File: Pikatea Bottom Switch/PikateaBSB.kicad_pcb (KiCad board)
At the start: 2 copper layers, 20 parts, among them J1 Micro_SD_Card, J2 Conn_01x15, SW1 Rotary_Encoder_Switch, U1 AMS1117-3.3, U2 74LVC125APW,118

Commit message: rudimentary layout
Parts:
- removed K?2: KEYSW, random-keyboard-parts:Generic-Mounthole
- moved SW1 50.3 mm to (115.2, 56.4)
- moved MX4 45.2 mm to (174.0, 59.6)
- moved MX2 45.2 mm to (153.8, 59.6)
- moved J2 36.8 mm to (172.2, 48.0), turned to 90 degrees
- moved C1 36.5 mm to (138.4, 58.2)
- moved C2 34.3 mm to (124.4, 48.0)
- moved C4 34.3 mm to (143.2, 43.1)
- moved K?1 34.3 mm to (143.8, 40.0)
- moved R3 34.3 mm to (128.8, 48.0)
- moved U1 34.3 mm to (127.1, 42.5)
- moved R2 27.7 mm to (162.1, 57.1)
- moved R4 27.7 mm to (166.5, 57.1)
- moved C3 27.2 mm to (161.1, 53.7)
- moved R1 27.2 mm to (165.5, 53.7)
- moved U2 16.0 mm to (154.2, 47.4)
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
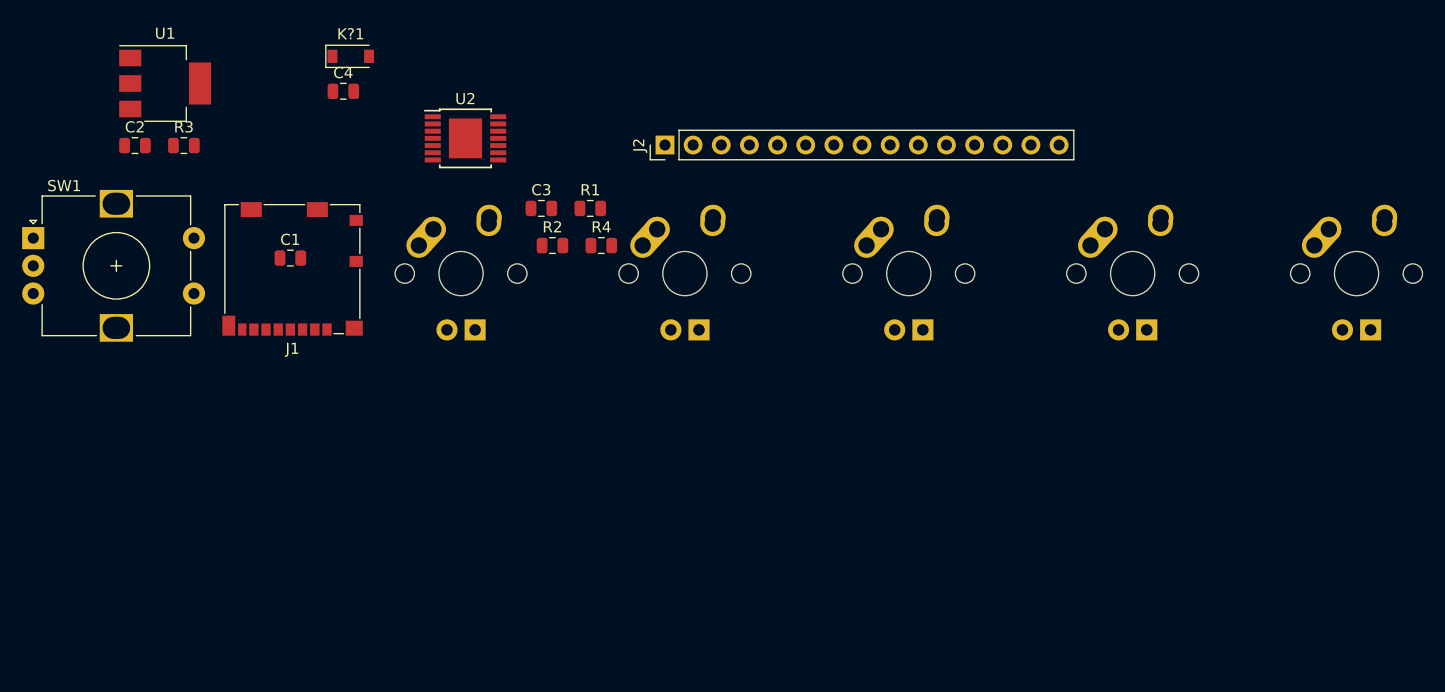
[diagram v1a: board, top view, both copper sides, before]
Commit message: Bottom Switch plate, footprints in place
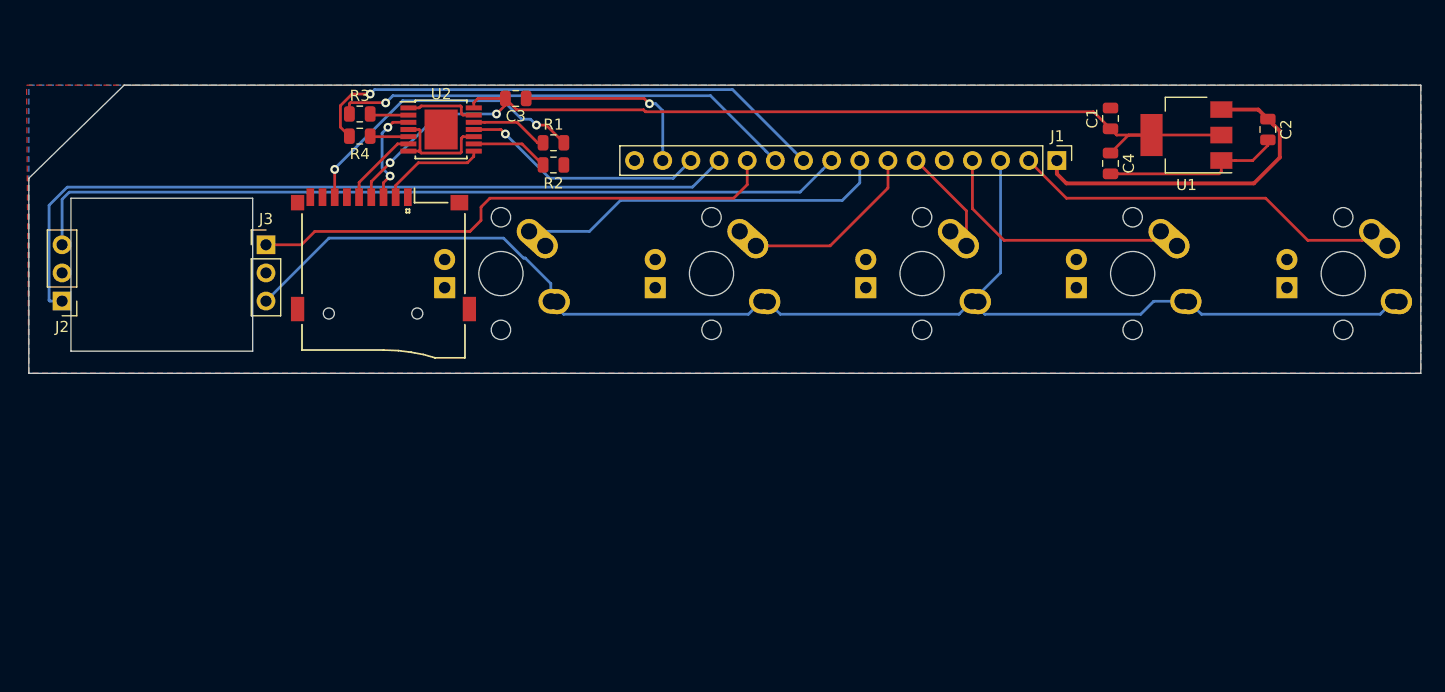
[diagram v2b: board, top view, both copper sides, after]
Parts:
- removed K?1: KEYSW, random-keyboard-parts:D_SOD-123-Pretty
- removed SW1: Rotary_Encoder_Switch, Rotary_Encoder:RotaryEncoder_Alps_EC12E-Switch_Vertical_H20mm
- added J3: Conn_01x03, Connector_PinHeader_2.54mm:PinHeader_1x03_P2.54mm_Vertical, F.Cu at (136.2, 57.0)
- added XS1: SD_ebay-uSD-push_push_SMD, Sd-Card:Conn_uSDcard, F.Cu at (146.8, 63.2)
- J1: value Micro_SD_Card -> Conn_01x16; footprint Connector_Card:microSD_HC_Molex_104031-0811 -> Connector_PinHeader_2.54mm:PinHeader_1x16_P2.54mm_Vertical
- J2: value Conn_01x15 -> Conn_01x03; footprint Connector_PinHeader_2.54mm:PinHeader_1x15_P2.54mm_Vertical -> Connector_PinHeader_2.54mm:PinHeader_1x03_P2.54mm_Vertical
- moved C2 102.2 mm to (226.6, 46.6), turned to 270 degrees
- moved U1 92.3 mm to (219.2, 47.1), turned to 180 degrees
- moved C1 75.1 mm to (212.4, 45.6), turned to 90 degrees
- moved J1 69.7 mm to (207.6, 49.4), turned to 270 degrees
- moved C4 69.5 mm to (212.4, 49.7), turned to 270 degrees
- moved J2 56.2 mm to (117.8, 62.1), turned to 180 degrees
- moved R4 23.9 mm to (144.7, 47.2)
- moved R3 16.1 mm to (144.7, 45.2)
- moved C3 10.2 mm to (158.7, 43.8)
- moved R2 7.27 mm to (162.1, 49.8), turned to 180 degrees
- moved R1 6.79 mm to (162.1, 47.8)
- moved MX2 3.60 mm to (157.4, 59.6), turned to 270 degrees
- moved MX4 2.40 mm to (176.4, 59.6), turned to 270 degrees
- moved U2 2.34 mm to (152.0, 46.6)
- moved MX1 1.20 mm to (195.4, 59.6), turned to 270 degrees
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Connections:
- J1 pad 1: Net-(J1-Pad1) -> /5v
- J1 pad 10: (no net) -> /SCK
- J1 pad 11: (no net) -> /MOSI
- J1 pad 2: Net-(J1-Pad2) -> /D7
- J1 pad 3: Net-(J1-Pad3) -> /A0
- J1 pad 4: /3.3V -> /D5
- J1 pad 5: Net-(J1-Pad5) -> /CS
- J1 pad 6: GND -> /D9
- J1 pad 7: Net-(J1-Pad7) -> /D8
- J1 pad 8: Net-(J1-Pad8) -> /D6
- J1 pad 9: Net-(J1-Pad9) -> /D4
- J2 pad 1: /5v -> /D3
- J2 pad 2: /Pin2 -> GND
- J2 pad 3: /Pin3 -> /D4
- MX1 pad 1: /Pin? -> /D9
- MX1 pad 2: /Pin? -> /A0
- MX2 pad 1: /Pin? -> /D6
- MX2 pad 2: /Pin? -> /A0
- MX3 pad 1: /Pin? -> /D5
- MX3 pad 2: /Pin? -> /A0
- MX4 pad 1: /Pin? -> /D8
- MX4 pad 2: /Pin? -> /A0
- MX5 pad 1: /Pin? -> /D7
- MX5 pad 2: /Pin? -> /A0
- R1 pad 2: Net-(J1-Pad7) -> Net-(R1-Pad2)
- R2 pad 1: /Pin? -> /CS
- R3 pad 1: /Pin? -> /MOSI
- R4 pad 1: /Pin? -> /SCK
- U2 pad 11: /Pin? -> /MISO
- U2 pad 3: Net-(J1-Pad3) -> Net-(U2-Pad3)
- U2 pad 6: Net-(J1-Pad5) -> Net-(U2-Pad6)
- U2 pad 8: Net-(J1-Pad2) -> Net-(U2-Pad8)
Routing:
- net /A0: track 0.00 -> 123.8 mm
- net /3.3V: track 0.00 -> 90.8 mm, vias 0 -> 2
- net /D4: track 0.00 -> 75.0 mm
- net /D3: track 0.00 -> 71.9 mm
- net GND: track 0.00 -> 50.6 mm, vias 0 -> 1
- net /D2: track 0.00 -> 48.5 mm
- net /SCK: track 0.00 -> 48.1 mm, vias 0 -> 1
- net /MOSI: track 0.00 -> 42.1 mm, vias 0 -> 1
- net /D7: track 0.00 -> 34.2 mm
- net /D6: track 0.00 -> 33.7 mm
- net /5v: track 0.00 -> 31.1 mm
- net Net-(R1-Pad2): track 0.00 -> 27.4 mm, vias 0 -> 2
- net /D5: track 0.00 -> 22.9 mm
- net /MISO: track 0.00 -> 22.1 mm, vias 0 -> 1
- net /D8: track 0.00 -> 16.6 mm
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- added copper zone on B.Cu, net GND
- added copper zone on F.Cu, net GND
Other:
- board outline added: 125.6 x 26 mm

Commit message: Update Doughter board
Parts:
- MX1, MX2, MX3, MX4, MX5: moved to B.Cu
- moved C3 1.67 mm to (158.6, 45.5), turned to 270 degrees
- moved U2 1.46 mm to (152.4, 48.0)
- moved R1 1.13 mm to (161.3, 47.0)
- moved R2 1.13 mm to (161.3, 49.0)
- turned MX1 to 90 degrees
- turned MX2 to 90 degrees
- turned MX3 to 90 degrees
- turned MX4 to 90 degrees
- turned MX5 to 90 degrees
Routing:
- net GND: track 50.6 -> 95.2 mm, vias 1 -> 2
- net /CS: track 0.00 -> 36.9 mm
- net /D9: track 9.58 -> 18.4 mm
- net /A0: track 123.8 -> 115.2 mm
- net /D7: track 34.2 -> 42.1 mm
- net /D8: track 16.6 -> 22.3 mm
- net /D5: track 22.9 -> 28.3 mm
- net /MOSI: track 42.1 -> 45.9 mm
- net /D3: track 71.9 -> 75.5 mm
- net /D6: track 33.7 -> 36.8 mm
- net Net-(U2-Pad8): track 9.66 -> 12.7 mm
- net Net-(U2-Pad3): track 9.39 -> 7.27 mm
- net Net-(R2-Pad2): track 7.04 -> 5.17 mm
- net Net-(R1-Pad1): track 7.02 -> 5.31 mm
- net Net-(R3-Pad2): track 3.49 -> 4.61 mm
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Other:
- board size 125.6 x 26 mm -> 125.6 x 25 mm

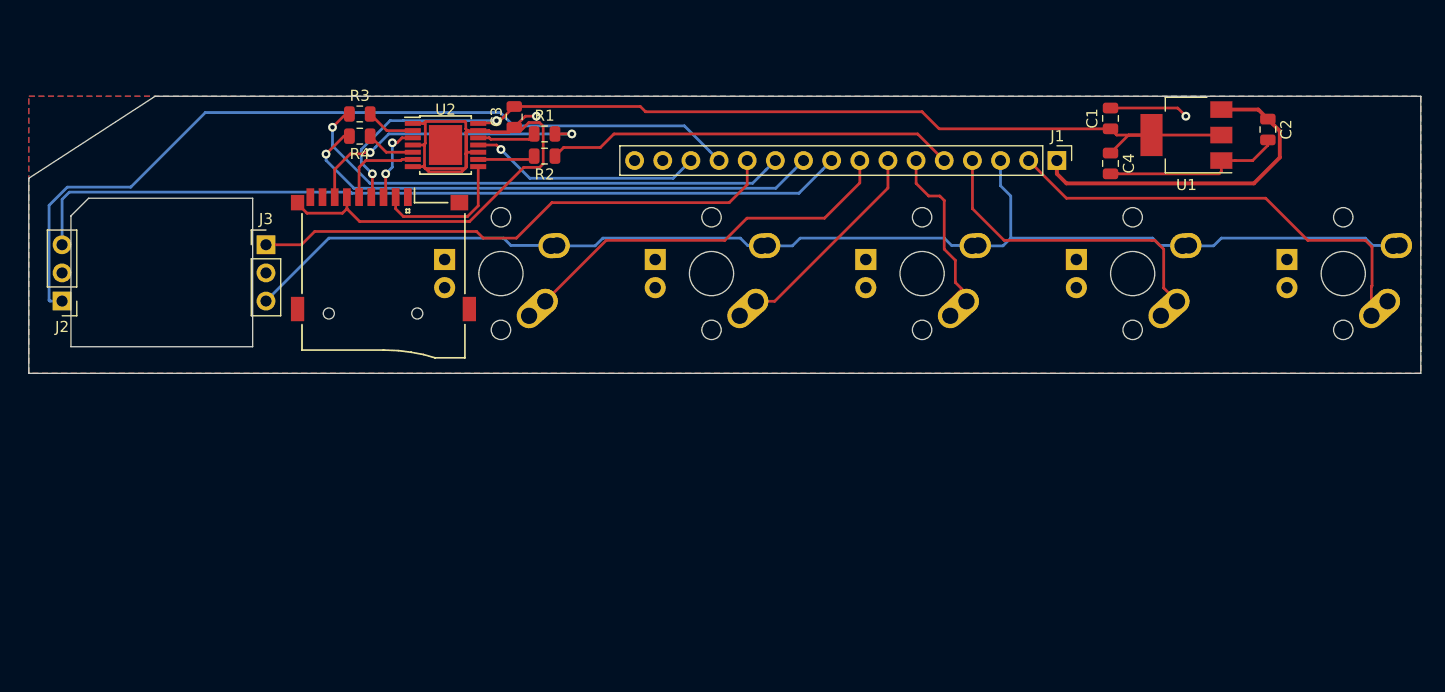
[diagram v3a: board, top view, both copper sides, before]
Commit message: added circuit board cutouts
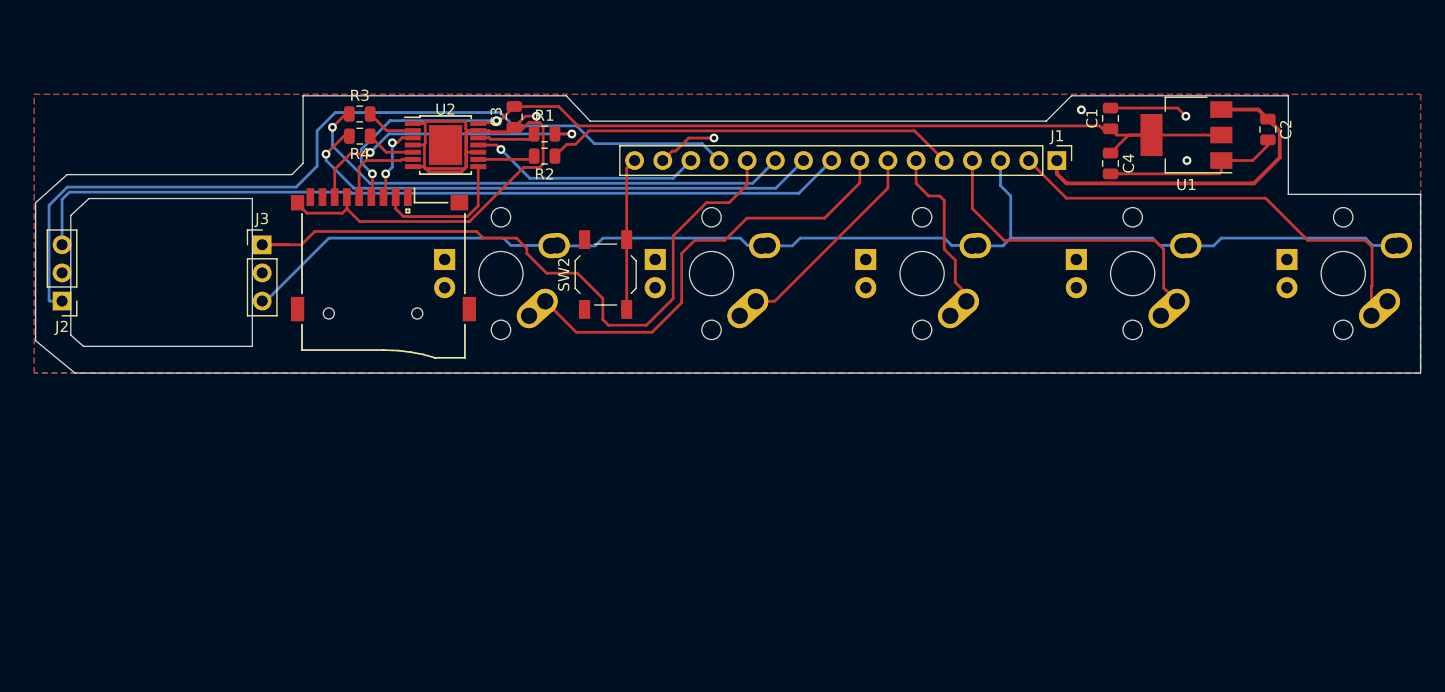
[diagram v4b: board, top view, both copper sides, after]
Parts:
- added SW2: SW_DPST, Button_Switch_SMD:SW_SPST_TL3342, F.Cu at (166.8, 59.7)
- moved J3 0.34 mm to (135.9, 57.0)
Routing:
- net /RESET: track 0.00 -> 13.7 mm
- net /D2: track 48.3 -> 61.9 mm
- net GND: track 95.2 -> 100.7 mm, vias 2 -> 5
- net /D6: track 36.8 -> 39.9 mm
- net /D3: track 75.5 -> 77.4 mm
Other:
- board size 125.6 x 25 mm -> 125 x 25 mm

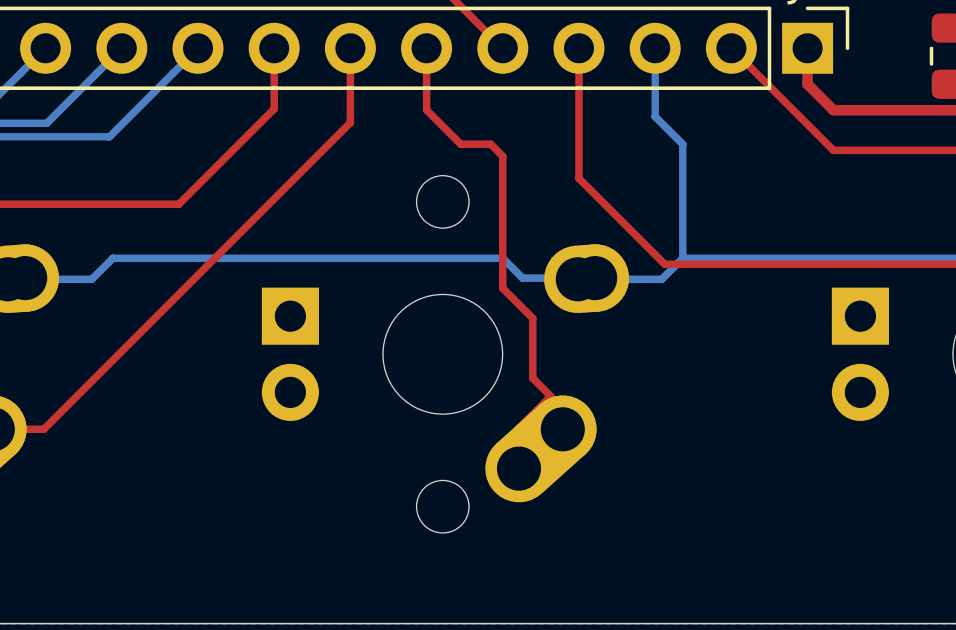
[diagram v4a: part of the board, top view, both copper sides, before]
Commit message: updated gerbers for daughter board
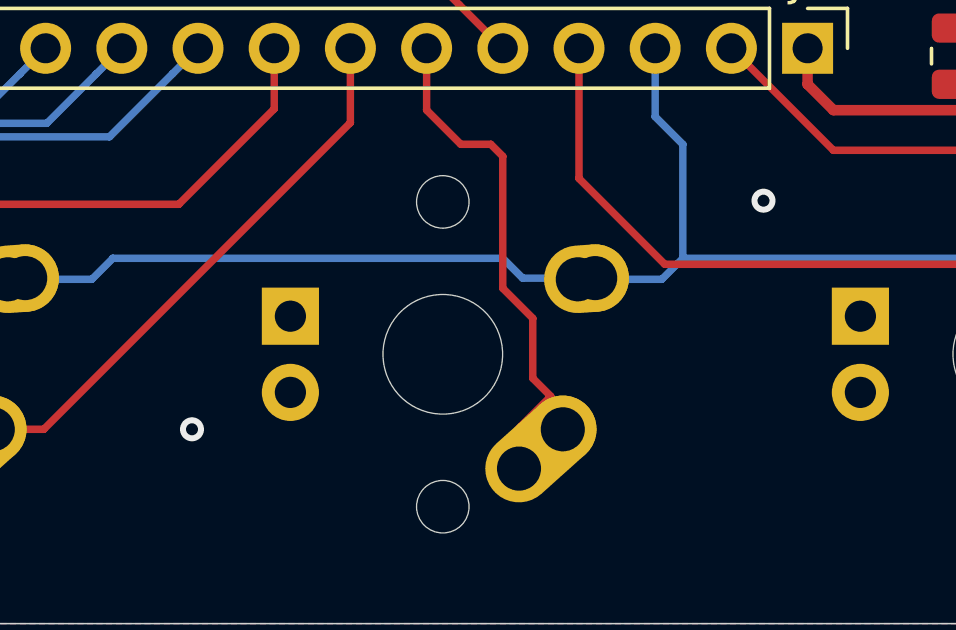
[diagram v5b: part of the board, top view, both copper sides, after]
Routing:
- net GND: vias 5 -> 7
